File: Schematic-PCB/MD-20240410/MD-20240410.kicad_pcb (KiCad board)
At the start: 2 copper layers, 100.5 x 56.4 mm, 49 parts, among them J3 Conn_01x02_Pin, J4 Conn_01x02_Pin, J5 Conn_01x02_Pin, J6 Conn_01x02_Pin, J8 Conn_01x15_Pin, Q3 NMOS, Q4 NMOS

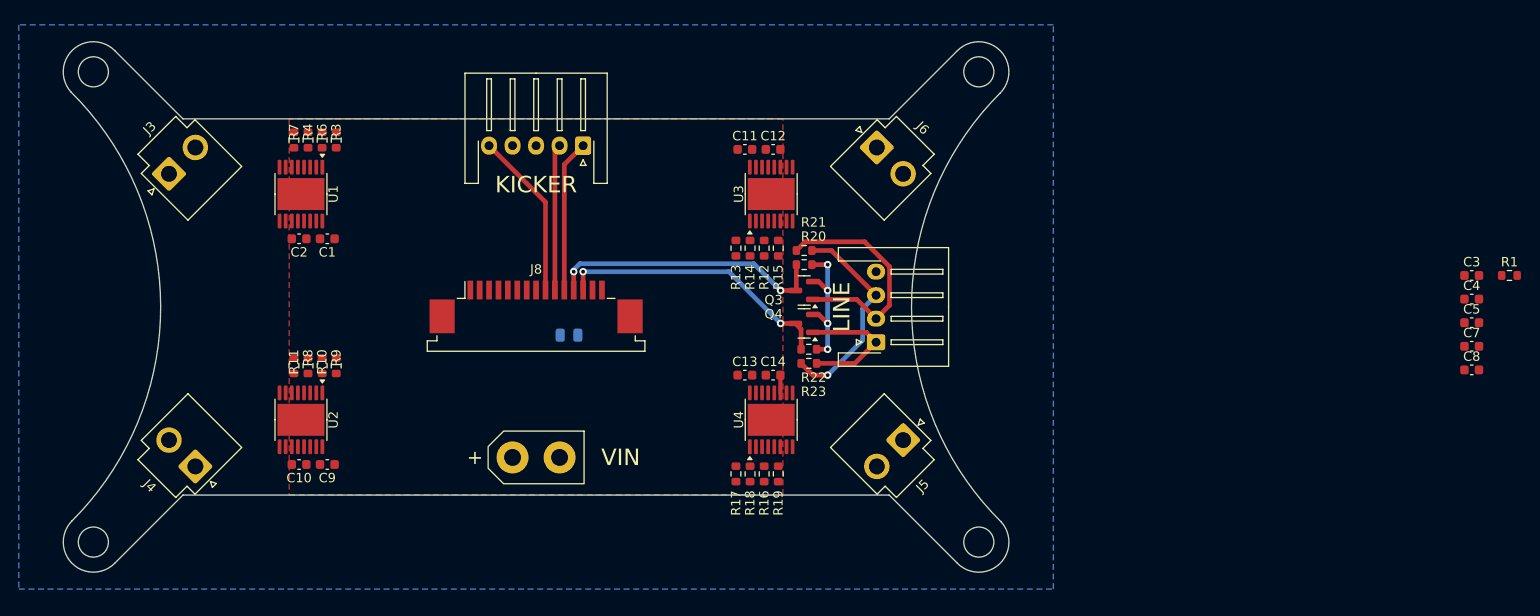
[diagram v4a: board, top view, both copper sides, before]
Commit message: MD基板のPCBを更新
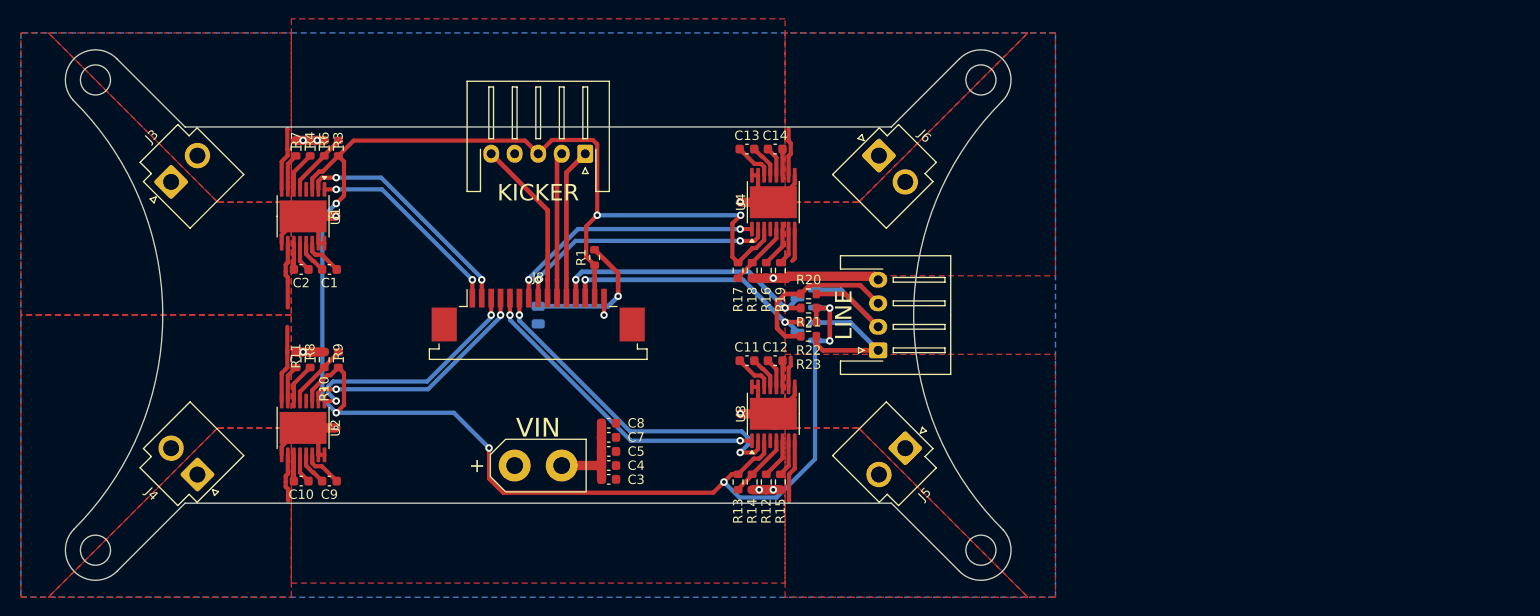
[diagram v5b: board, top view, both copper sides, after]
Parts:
- Q3, Q4: moved to B.Cu
- moved R1 97.3 mm to (6.22, -5.26), turned to 90 degrees
- moved C3 94.3 mm to (7.72, 18.3), turned to 180 degrees
- moved C4 93.4 mm to (7.72, 16.9), turned to 180 degrees
- moved C5 92.8 mm to (7.72, 15.4), turned to 180 degrees
- moved C7 92.3 mm to (7.72, 13.9), turned to 180 degrees
- moved C8 91.9 mm to (7.72, 12.4), turned to 180 degrees
- moved R12 24.9 mm to (24.5, 18.6)
- moved R13 24.9 mm to (21.5, 18.6)
- moved R14 24.9 mm to (23.0, 18.6)
- moved R15 24.9 mm to (26.0, 18.6)
- moved C13 24.0 mm to (22.4, -16.8)
- moved C14 24.0 mm to (25.4, -16.8)
- moved U3 23.4 mm to (25.2, 11.4)
- moved U4 23.1 mm to (25.2, -11.1)
- moved C11 22.5 mm to (22.4, 5.71)
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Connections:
- J3 pad 1: OUT1-1 -> OUT2-1
- J3 pad 2: OUT2-1 -> OUT1-1
- J4 pad 1: OUT1-2 -> OUT2-2
- J4 pad 2: OUT2-2 -> OUT1-2
- J5 pad 1: OUT1-3 -> OUT2-3
- J5 pad 2: OUT2-3 -> OUT1-3
- J6 pad 1: OUT1-4 -> OUT2-4
- J6 pad 2: OUT2-4 -> OUT1-4
- VIN pad 1: VCC -> VM
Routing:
- net SLEEP-1: track 15.8 -> 205.3 mm, vias 4 -> 8
- net GND: track 0.00 -> 81.3 mm, vias 0 -> 11
- net PH-3: track 0.00 -> 36.7 mm, vias 0 -> 2
- net EN-3: track 0.00 -> 33.4 mm, vias 0 -> 2
- net PH-4: track 0.00 -> 28.2 mm, vias 0 -> 2
- net EN-4: track 0.00 -> 28.0 mm, vias 0 -> 2
- net PH-2: track 0.00 -> 25.6 mm, vias 0 -> 2
- net EN-2: track 0.00 -> 25.6 mm, vias 0 -> 2
- net PH-1: track 0.00 -> 25.0 mm, vias 0 -> 2
- net EN-1: track 0.00 -> 21.7 mm, vias 0 -> 2
- net Net-(D1-A): track 0.00 -> 14.9 mm, vias 0 -> 1
- net VM: track 1.89 -> 11.2 mm
- net Line-MD-Main=RX_5V: track 25.1 -> 16.4 mm
- net OUT1-2: track 0.00 -> 8.14 mm
- net OUT2-1: track 0.00 -> 7.02 mm
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- added copper zone on F.Cu, net OUT1-1
- added copper zone on F.Cu, net OUT1-2
- added copper zone on F.Cu, net OUT1-3
- added copper zone on F.Cu, net OUT1-4
- added copper zone on F.Cu, net OUT2-1
- added copper zone on F.Cu, net OUT2-2
- added copper zone on F.Cu, net OUT2-3
- added copper zone on F.Cu, net OUT2-4

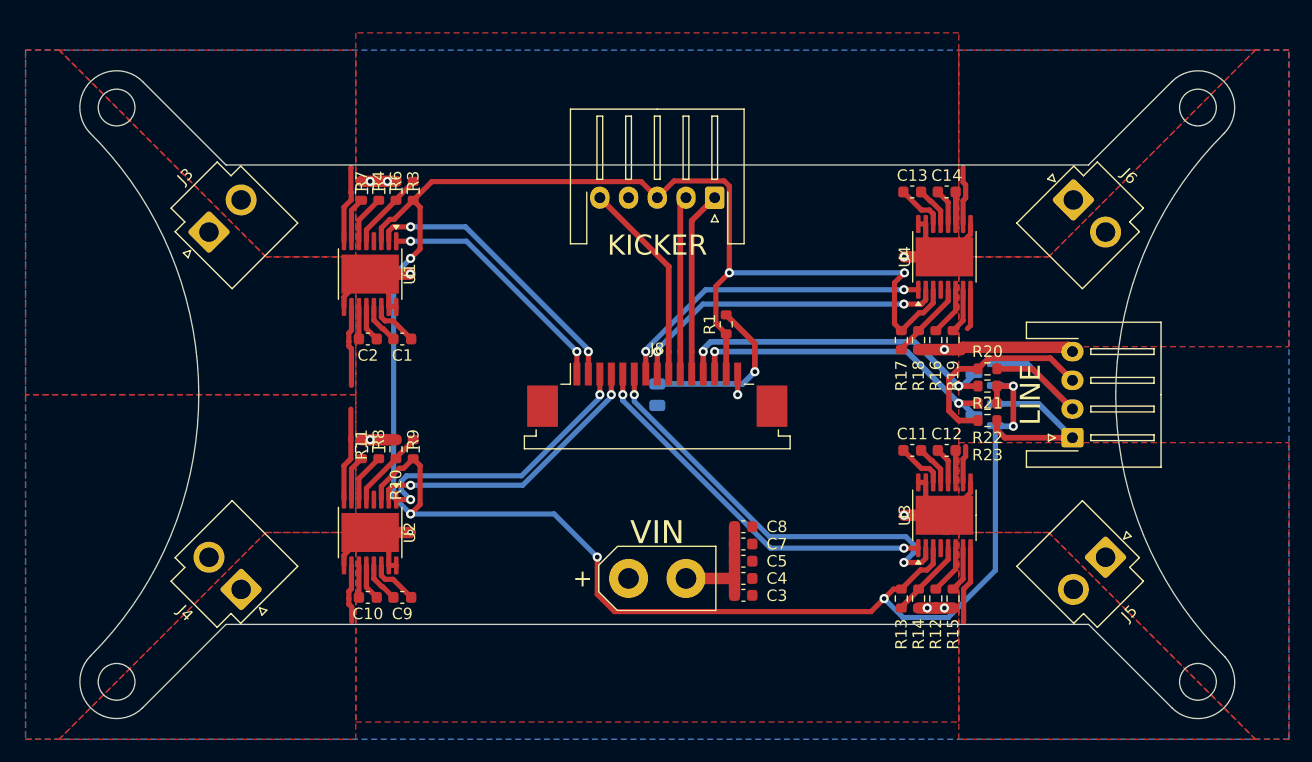
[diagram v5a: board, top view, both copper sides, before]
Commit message: MD基板の基板外形などを更新、仮DRしたよ
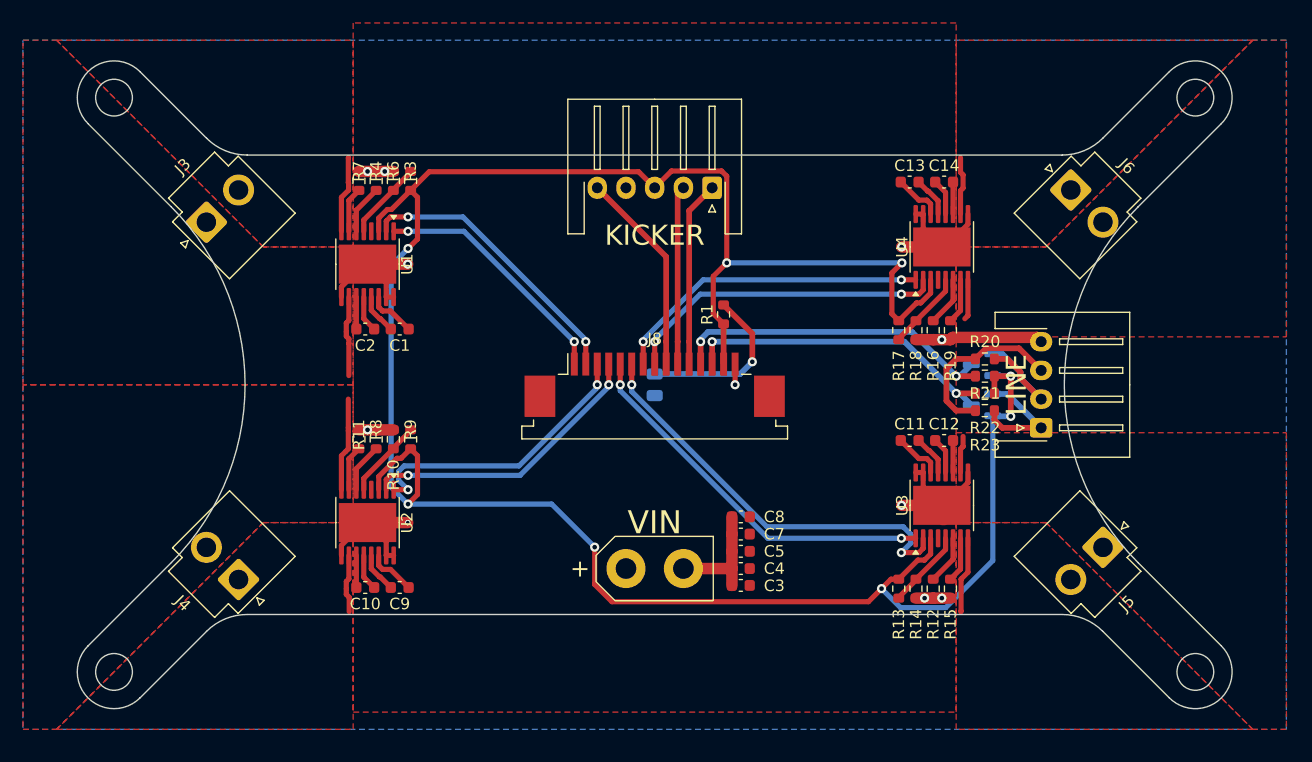
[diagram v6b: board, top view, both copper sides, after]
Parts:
- moved LINE 2.86 mm to (33.6, 3.75)
- moved C11 0.89 mm to (22.2, 4.85)
- moved C12 0.89 mm to (25.2, 4.85)
- moved J3 0.89 mm to (-37.6, -15.6)
- moved J4 0.89 mm to (-37.6, 15.6)
- moved J5 0.89 mm to (37.6, 15.6)
- moved J6 0.89 mm to (37.6, -15.6)
- moved R12 0.89 mm to (24.2, 17.8)
- moved R13 0.89 mm to (21.2, 17.8)
- moved R14 0.89 mm to (22.8, 17.8)
- moved R15 0.89 mm to (25.8, 17.8)
- moved R3 0.89 mm to (-21.2, -17.8)
- moved R4 0.89 mm to (-24.2, -17.8)
- moved R6 0.89 mm to (-22.8, -17.8)
- moved R7 0.89 mm to (-25.8, -17.8)
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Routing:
- net Line-MD-Main=TX_5V: track 15.6 -> 10.6 mm
- net Line-MD-Main=RX_5V: track 16.4 -> 12.0 mm
- net GND: track 81.3 -> 78.8 mm
- net +5V: track 18.0 -> 15.5 mm
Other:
- outline, holes or cut-outs redrawn

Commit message: MDのDRしたよ
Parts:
- removed KICKER: Conn_01x05_Pin, Connector_JST:JST_XH_S5B-XH-A-1_1x05_P2.50mm_Horizontal
- removed LINE: Conn_01x04_Pin, Connector_JST:JST_XH_S4B-XH-A-1_1x04_P2.50mm_Horizontal
- added J1: Conn_01x05_Pin, Connector_JST:JST_XH_S5B-XH-A-1_1x05_P2.50mm_Horizontal, F.Cu at (5.00, -17.1)
- added J2: Conn_01x04_Pin, Connector_JST:JST_XH_S4B-XH-A-1_1x04_P2.50mm_Horizontal, F.Cu at (33.8, 3.75)
- moved R22 1.50 mm to (28.8, 2.25)
- moved R23 1.50 mm to (28.8, 0.75)
- moved Q3 0.20 mm to (28.5, -1.55)
- renumbered VIN to J7
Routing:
- net Line-MD-Main=RX_5V: track 12.0 -> 6.43 mm, vias 0 -> 1
- net Line-MD-Main=TX_5V: track 10.6 -> 6.11 mm, vias 0 -> 1
- net GND: track 78.8 -> 76.0 mm
- net +5V: track 15.5 -> 16.9 mm
- net Line-MD-Main=RX_3.3V: track 29.7 -> 30.3 mm

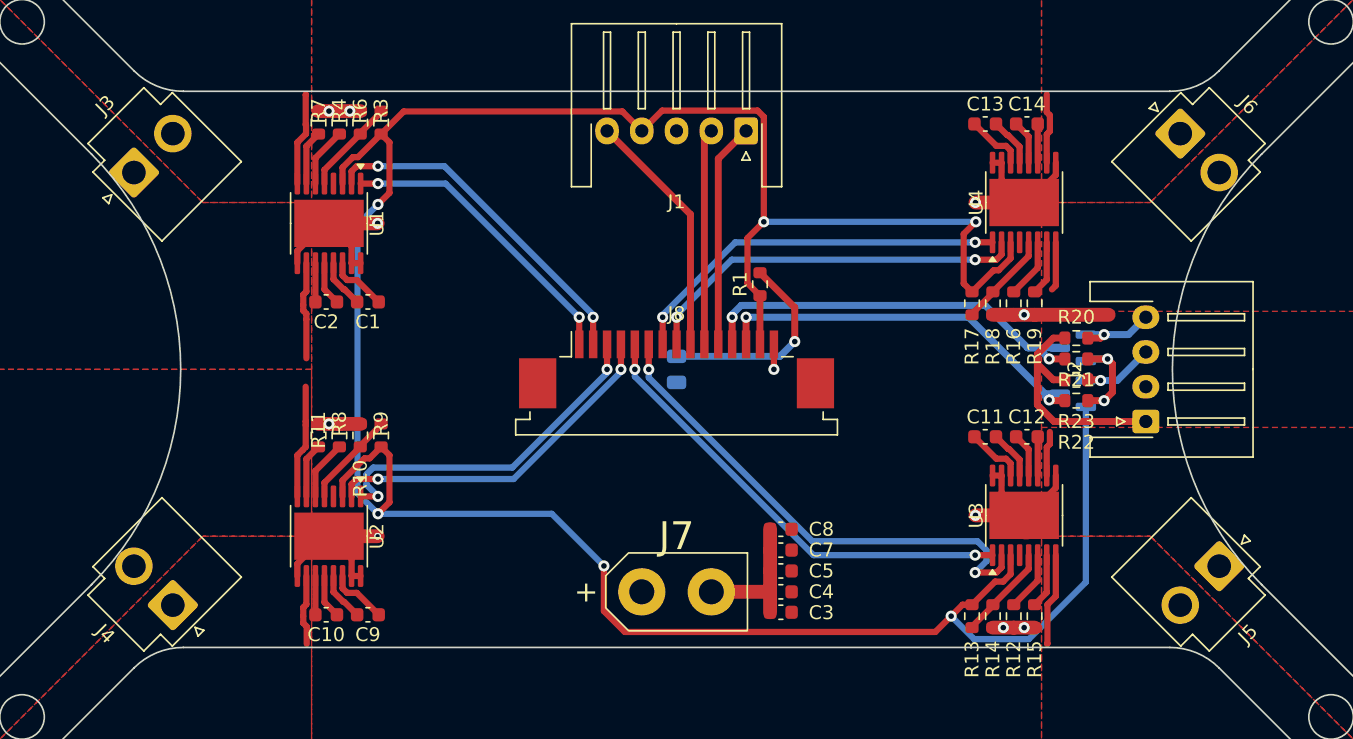
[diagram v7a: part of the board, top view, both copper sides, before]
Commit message: MD基板を修正したよ
XH4ピンの位置を裏側・内側へ直した
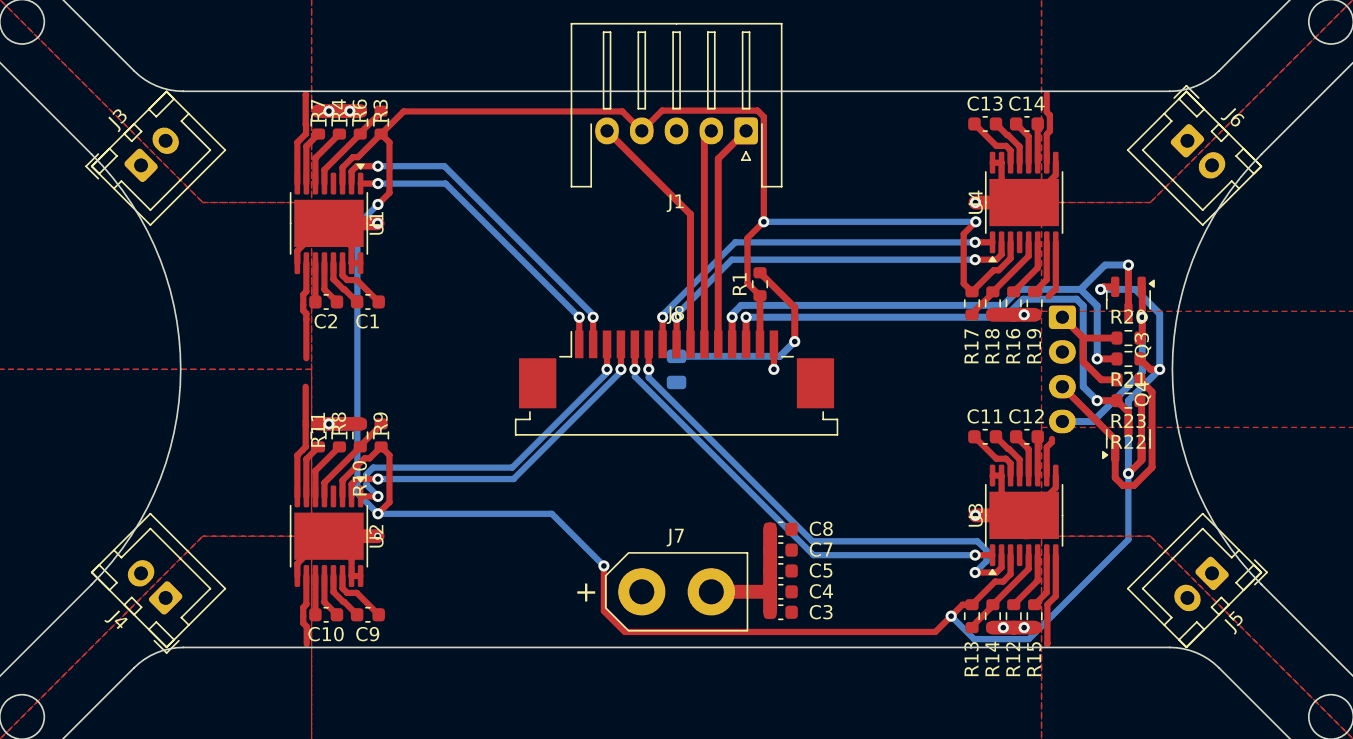
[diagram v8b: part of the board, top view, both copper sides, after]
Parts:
- J2: moved to B.Cu
- J3, J4, J5, J6: footprint @2024-MD:JST_VH_B2P-VH-B_1x02_P3.96mm_Vertical -> @2024TOINIOT2-MD:JST_XH_B2B-XH-A_1x02_P2.50mm_Vertical
- J7: footprint @2024-MD:XT30U-M -> @2024TOINIOT2-MD:XT30U-M
- Q3, Q4: moved to F.Cu
- moved J2 9.60 mm to (27.8, -3.75), turned to -90 degrees
- moved Q3 5.28 mm to (32.5, -5.00), turned to -90 degrees
- moved Q4 5.15 mm to (32.5, 5.00), turned to 90 degrees
- moved R20 3.75 mm to (32.5, -0.75)
- moved R21 3.75 mm to (32.5, -2.25)
- moved R22 3.75 mm to (32.5, 2.25)
- moved R23 3.75 mm to (32.5, 0.75)
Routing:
- net SLEEP-1: track 204.8 -> 218.3 mm, vias 8 -> 9
- net Line-MD-Main=TX_5V: track 6.11 -> 18.5 mm, vias 1 -> 0
- net Line-MD-Main=RX_3.3V: track 30.3 -> 42.5 mm, vias 2 -> 3
- net Line-MD-Main=TX_3.3V: track 28.9 -> 37.8 mm
- net Line-MD-Main=RX_5V: track 6.43 -> 15.0 mm
- net +5V: track 16.9 -> 9.21 mm
- net GND: track 76.0 -> 70.6 mm
- net OUT1-4: track 3.50 -> 4.10 mm
